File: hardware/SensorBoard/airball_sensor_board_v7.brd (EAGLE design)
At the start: 139.7 x 38.1 mm, 24 parts, among them J1 FEMALE 2x3

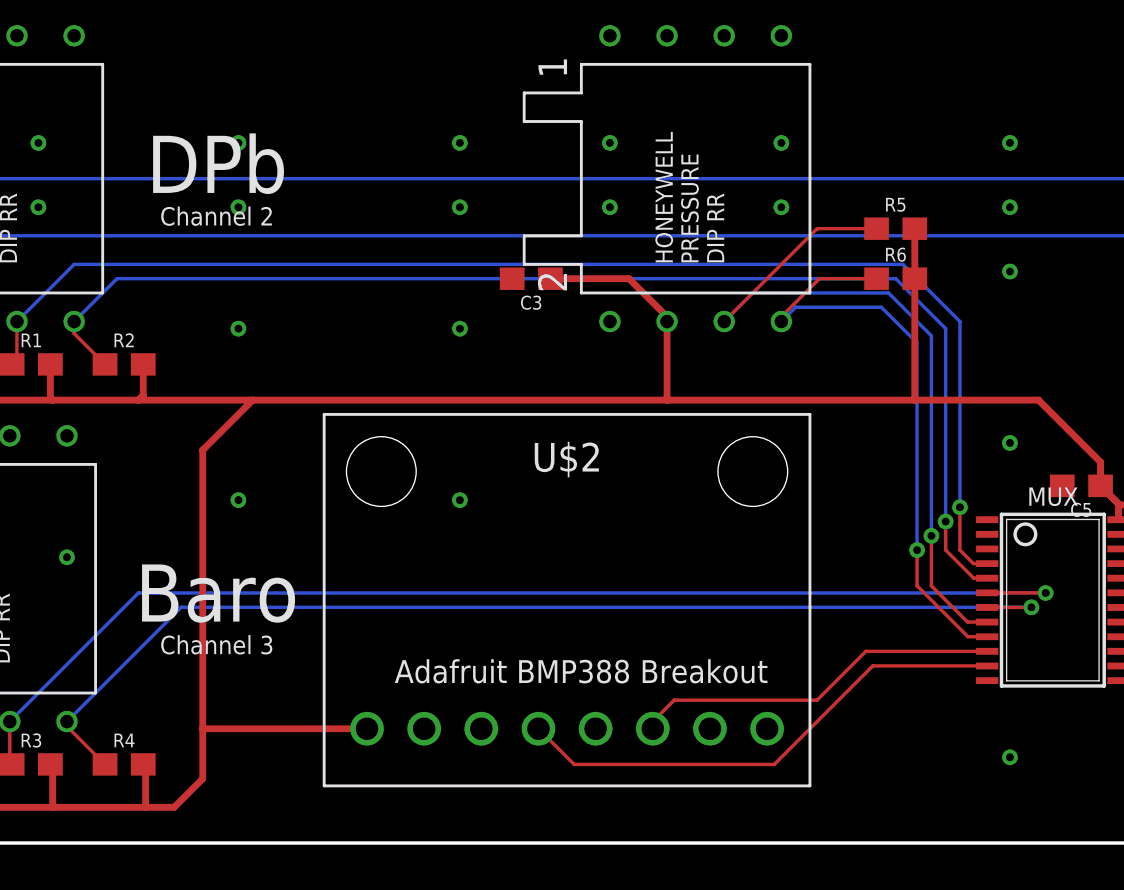
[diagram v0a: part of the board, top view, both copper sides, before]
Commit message: Moved BMP388 breakout to allow more space for plumbing.
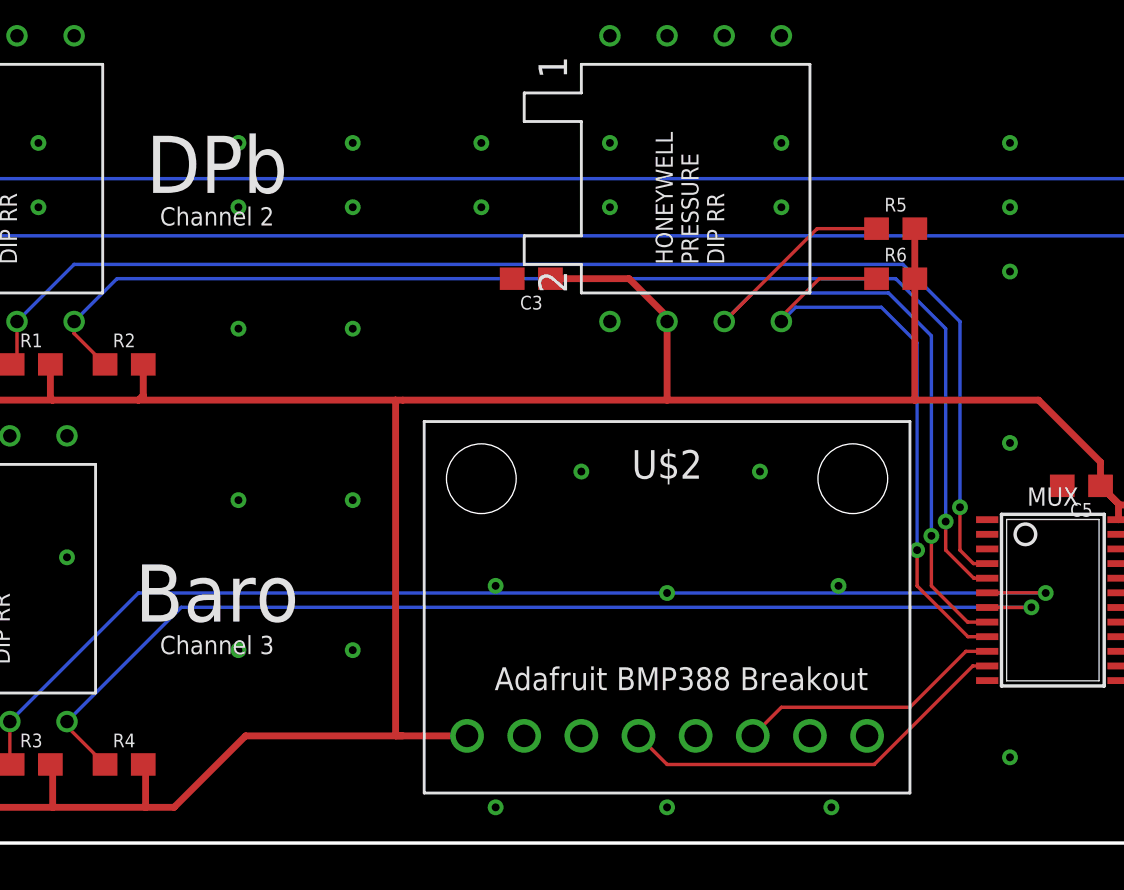
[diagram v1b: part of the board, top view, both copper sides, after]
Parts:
- moved U$2 4.46 mm to (60.3, 2.22)
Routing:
- net SCL_BMP_BARO: track 22.4 -> 17.8 mm
- net SDA_BMP_BARO: track 16.5 -> 12.0 mm
- net VCC_3V3: track 184.3 -> 187.0 mm
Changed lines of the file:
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@@
 <attribute name="VALUE" x="98.552" y="34.925" size="0.6096" layer="27" font="vector" ratio="20" rot="R270"/>
 </element>
-<element name="U$2" library="airball" package="ADAFRUIT_BMP388_BREAKOUT" value="ADAFRUIT_BMP388_BREAKOUT" x="55.88" y="2.54" smashed="yes">
-<attribute name="NAME" x="66.675" y="17.145" size="1.27" layer="25" align="center"/>
-<attribute name="VALUE" x="66.675" y="13.97" size="1.27" layer="27" align="center"/>
+<element name="U$2" library="airball" package="ADAFRUIT_BMP388_BREAKOUT" value="ADAFRUIT_BMP388_BREAKOUT" x="60.325" y="2.2225" smashed="yes">
+<attribute name="NAME" x="71.12" y="16.8275" size="1.27" layer="25" align="center"/>
+<attribute name="VALUE" x="71.12" y="13.6525" size="1.27" layer="27" align="center"/>
 </element>
 </elements>
@@
 <contactref element="MUX" pad="10"/>
 <contactref element="U$2" pad="P$6"/>
-<wire x1="85.3472" y1="8.52" x2="79.9575" y2="8.52" width="0.1524" layer="1"/>
-<wire x1="79.9575" y1="8.52" x2="77.7875" y2="6.35" width="0.1524" layer="1"/>
-<wire x1="77.7875" y1="6.35" x2="71.4375" y2="6.35" width="0.1524" layer="1"/>
-<wire x1="71.4375" y1="6.35" x2="70.485" y2="5.3975" width="0.1524" layer="1"/>
-<wire x1="70.485" y1="5.3975" x2="70.485" y2="5.08" width="0.1524" layer="1"/>
+<wire x1="85.3472" y1="8.52" x2="84.4025" y2="8.52" width="0.1524" layer="1"/>
+<wire x1="84.4025" y1="8.52" x2="81.915" y2="6.0325" width="0.1524" layer="1"/>
+<wire x1="81.915" y1="6.0325" x2="76.2" y2="6.0325" width="0.1524" layer="1"/>
+<wire x1="76.2" y1="6.0325" x2="74.93" y2="4.7625" width="0.1524" layer="1"/>
 </signal>
 <signal name="SCL_BMP_BARO">
 <contactref element="MUX" pad="11"/>
 <contactref element="U$2" pad="P$4"/>
-<wire x1="85.3472" y1="7.87" x2="80.26" y2="7.87" width="0.1524" layer="1"/>
-<wire x1="80.26" y1="7.87" x2="75.8825" y2="3.4925" width="0.1524" layer="1"/>
-<wire x1="75.8825" y1="3.4925" x2="66.9925" y2="3.4925" width="0.1524" layer="1"/>
-<wire x1="66.9925" y1="3.4925" x2="65.405" y2="5.08" width="0.1524" layer="1"/>
+<wire x1="85.3472" y1="7.87" x2="84.705" y2="7.87" width="0.1524" layer="1"/>
+<wire x1="84.705" y1="7.87" x2="80.3275" y2="3.4925" width="0.1524" layer="1"/>
+<wire x1="80.3275" y1="3.4925" x2="71.12" y2="3.4925" width="0.1524" layer="1"/>
+<wire x1="71.12" y1="3.4925" x2="69.85" y2="4.7625" width="0.1524" layer="1"/>
 </signal>
 <signal name="GND" class="1">
@@
 <wire x1="47.84" y1="3.4925" x2="47.9425" y2="3.39" width="0.3048" layer="1"/>
 <wire x1="47.9425" y1="3.39" x2="47.9425" y2="1.5875" width="0.3048" layer="1"/>
-<wire x1="49.2125" y1="1.5875" x2="50.4825" y2="2.8575" width="0.3048" layer="1"/>
+<wire x1="49.2125" y1="1.5875" x2="52.3875" y2="4.7625" width="0.3048" layer="1"/>
 <wire x1="90.385" y1="15.875" x2="90.385" y2="16.93" width="0.3048" layer="1"/>
 <wire x1="90.385" y1="16.93" x2="87.63" y2="19.685" width="0.3048" layer="1"/>
 <wire x1="87.63" y1="19.685" x2="82.13" y2="19.685" width="0.3048" layer="1"/>
 <wire x1="82.13" y1="19.685" x2="71.12" y2="19.685" width="0.3048" layer="1"/>
-<wire x1="71.12" y1="19.685" x2="52.705" y2="19.685" width="0.3048" layer="1"/>
-<wire x1="52.705" y1="19.685" x2="47.625" y2="19.685" width="0.3048" layer="1"/>
+<wire x1="71.12" y1="19.685" x2="59.3725" y2="19.685" width="0.3048" layer="1"/>
+<wire x1="59.3725" y1="19.685" x2="59.055" y2="19.685" width="0.3048" layer="1"/>
 <wire x1="47.625" y1="19.685" x2="43.815" y2="19.685" width="0.3048" layer="1"/>
 <wire x1="43.815" y1="19.685" x2="41.1725" y2="19.685" width="0.3048" layer="1"/>
@@
 <wire x1="43.7125" y1="19.7875" x2="43.815" y2="19.685" width="0.3048" layer="1"/>
 <wire x1="82.13" y1="25.0825" x2="82.13" y2="19.685" width="0.3048" layer="1"/>
-<wire x1="50.4825" y1="2.8575" x2="50.4825" y2="5.08" width="0.3048" layer="1"/>
-<wire x1="50.4825" y1="5.08" x2="50.4825" y2="17.4625" width="0.3048" layer="1"/>
-<wire x1="50.4825" y1="17.4625" x2="52.705" y2="19.685" width="0.3048" layer="1"/>
+<wire x1="52.3875" y1="4.7625" x2="59.3725" y2="4.7625" width="0.3048" layer="1"/>
+<wire x1="59.055" y1="4.7625" x2="59.055" y2="19.685" width="0.3048" layer="1"/>
 <wire x1="107.95" y1="12.7" x2="113.17486875" y2="12.7" width="0.3048" layer="1"/>
 <wire x1="113.17486875" y1="12.7" x2="113.78446875" y2="12.0904" width="0.3048" layer="1"/>
@@
 <wire x1="71.12" y1="23.3925" x2="69.43" y2="25.0825" width="0.3048" layer="1"/>
 <wire x1="69.43" y1="25.0825" x2="65.9375" y2="25.0825" width="0.3048" layer="1"/>
-<wire x1="57.785" y1="5.08" x2="50.4825" y2="5.08" width="0.3048" layer="1"/>
+<wire x1="62.23" y1="4.7625" x2="59.055" y2="4.7625" width="0.3048" layer="1"/>
+<wire x1="47.625" y1="19.685" x2="59.055" y2="19.685" width="0.3048" layer="1"/>
+<wire x1="59.3725" y1="4.7625" x2="59.055" y2="4.7625" width="0" layer="19" extent="1-1"/>
 </signal>
 <signal name="ARDUINO_TX">
@@
 </signal>
 <signal name="GND35" class="1">
-<via x="61.9125" y="31.115" extent="1-16" drill="0.35"/>
+<via x="57.15" y="31.115" extent="1-16" drill="0.35"/>
 </signal>
 <signal name="GND36" class="1">
@@
 </signal>
 <signal name="GND38" class="1">
-<via x="61.9125" y="15.24" extent="1-16" drill="0.35"/>
+<via x="57.15" y="15.24" extent="1-16" drill="0.35"/>
 </signal>
 <signal name="GND39" class="1">
@@
 </signal>
 <signal name="GND40" class="1">
-<via x="61.9125" y="22.86" extent="1-16" drill="0.35"/>
+<via x="57.15" y="22.86" extent="1-16" drill="0.35"/>
 </signal>
 <signal name="GND41" class="1">
@@
 </signal>
 <signal name="GND68" class="1">
-<via x="61.9125" y="28.2575" extent="1-16" drill="0.35"/>
+<via x="57.15" y="28.2575" extent="1-16" drill="0.35"/>
 </signal>
 <signal name="GND69" class="1">
@@
 <via x="34.925" y="24.765" extent="1-16" drill="0.35"/>
 </signal>
+<signal name="GND63" class="1">
+<via x="62.865" y="31.115" extent="1-16" drill="0.35"/>
+</signal>
+<signal name="GND74" class="1">
+<via x="62.865" y="28.2575" extent="1-16" drill="0.35"/>
+</signal>
+<signal name="GND75" class="1">
+<via x="57.15" y="8.5725" extent="1-16" drill="0.35"/>
+</signal>
+<signal name="GND76" class="1">
+<via x="52.07" y="8.5725" extent="1-16" drill="0.35"/>
+</signal>
+<signal name="GND77" class="1">
+<via x="67.31" y="16.51" extent="1-16" drill="0.35"/>
+</signal>
+<signal name="GND78" class="1">
+<via x="75.2475" y="16.51" extent="1-16" drill="0.35"/>
+</signal>
+<signal name="GND79" class="1">
+<via x="63.5" y="11.43" extent="1-16" drill="0.35"/>
+</signal>
+<signal name="GND80" class="1">
+<via x="78.74" y="11.43" extent="1-16" drill="0.35"/>
+</signal>
+<signal name="GND81" class="1">
+<via x="63.5" y="1.5875" extent="1-16" drill="0.35"/>
+</signal>
+<signal name="GND82" class="1">
+<via x="78.4225" y="1.5875" extent="1-16" drill="0.35"/>
+</signal>
+<signal name="GND83" class="1">
+<via x="71.12" y="1.5875" extent="1-16" drill="0.35"/>
+</signal>
+<signal name="GND84" class="1">
+<via x="71.12" y="11.1125" extent="1-16" drill="0.35"/>
+</signal>
 </signals>

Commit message: Updated V7 board schematics
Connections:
- net VCC_3V3: now also MUX.3
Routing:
- net VCC_3V3: track 187.0 -> 192.1 mm
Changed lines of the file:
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@@
 <wire x1="98.425" y1="15.025" x2="97.0525" y2="13.6525" width="0.3048" layer="1"/>
 <wire x1="97.0525" y1="13.6525" x2="97.0525" y2="11.1125" width="0.3048" layer="1"/>
-<wire x1="90.385" y1="15.875" x2="91.1828" y2="15.0772" width="0.3048" layer="1"/>
+<wire x1="90.43625" y1="15.82375" x2="91.1828" y2="15.0772" width="0.3048" layer="1"/>
 <wire x1="91.1828" y1="15.0772" x2="91.1828" y2="14.37" width="0.3048" layer="1"/>
 <wire x1="100.6475" y1="15.025" x2="91.235" y2="15.025" width="0.3048" layer="1"/>
-<wire x1="91.235" y1="15.025" x2="90.385" y2="15.875" width="0.3048" layer="1"/>
+<wire x1="91.235" y1="15.025" x2="91.1828" y2="15.0772" width="0.3048" layer="1"/>
+<wire x1="90.43625" y1="15.82375" x2="90.385" y2="15.875" width="0.3048" layer="1"/>
 <wire x1="39.585" y1="21.2725" x2="39.9025" y2="21.59" width="0.3048" layer="1"/>
 <wire x1="39.6875" y1="23.1775" x2="39.9025" y2="22.9625" width="0.3048" layer="1"/>
@@
 <wire x1="87.63" y1="19.685" x2="82.13" y2="19.685" width="0.3048" layer="1"/>
 <wire x1="82.13" y1="19.685" x2="71.12" y2="19.685" width="0.3048" layer="1"/>
-<wire x1="71.12" y1="19.685" x2="59.3725" y2="19.685" width="0.3048" layer="1"/>
-<wire x1="59.3725" y1="19.685" x2="59.055" y2="19.685" width="0.3048" layer="1"/>
+<wire x1="71.12" y1="19.685" x2="59.055" y2="19.685" width="0.3048" layer="1"/>
 <wire x1="47.625" y1="19.685" x2="43.815" y2="19.685" width="0.3048" layer="1"/>
 <wire x1="43.815" y1="19.685" x2="41.1725" y2="19.685" width="0.3048" layer="1"/>
@@
 <wire x1="62.23" y1="4.7625" x2="59.055" y2="4.7625" width="0.3048" layer="1"/>
 <wire x1="47.625" y1="19.685" x2="59.055" y2="19.685" width="0.3048" layer="1"/>
+<contactref element="MUX" pad="3"/>
+<wire x1="85.3472" y1="13.07" x2="87.6825" y2="13.07" width="0.3048" layer="1"/>
+<wire x1="87.6825" y1="13.07" x2="90.43625" y2="15.82375" width="0.3048" layer="1"/>
 <wire x1="59.3725" y1="4.7625" x2="59.055" y2="4.7625" width="0" layer="19" extent="1-1"/>
 </signal>
